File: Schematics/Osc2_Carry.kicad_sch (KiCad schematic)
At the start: 43 parts, among them J16 Conn_01x10h, J17 Screw_Terminal_01x03, J54 Screw_Terminal_01x03, J55 Conn_01x10h, J56 Conn_01x04, J59 Conn_01x04, J60 Conn_01x04, U101 LME49720N, U105 LM358, U12 LM358, U13 TL072, U14 LM358, U15 TL072

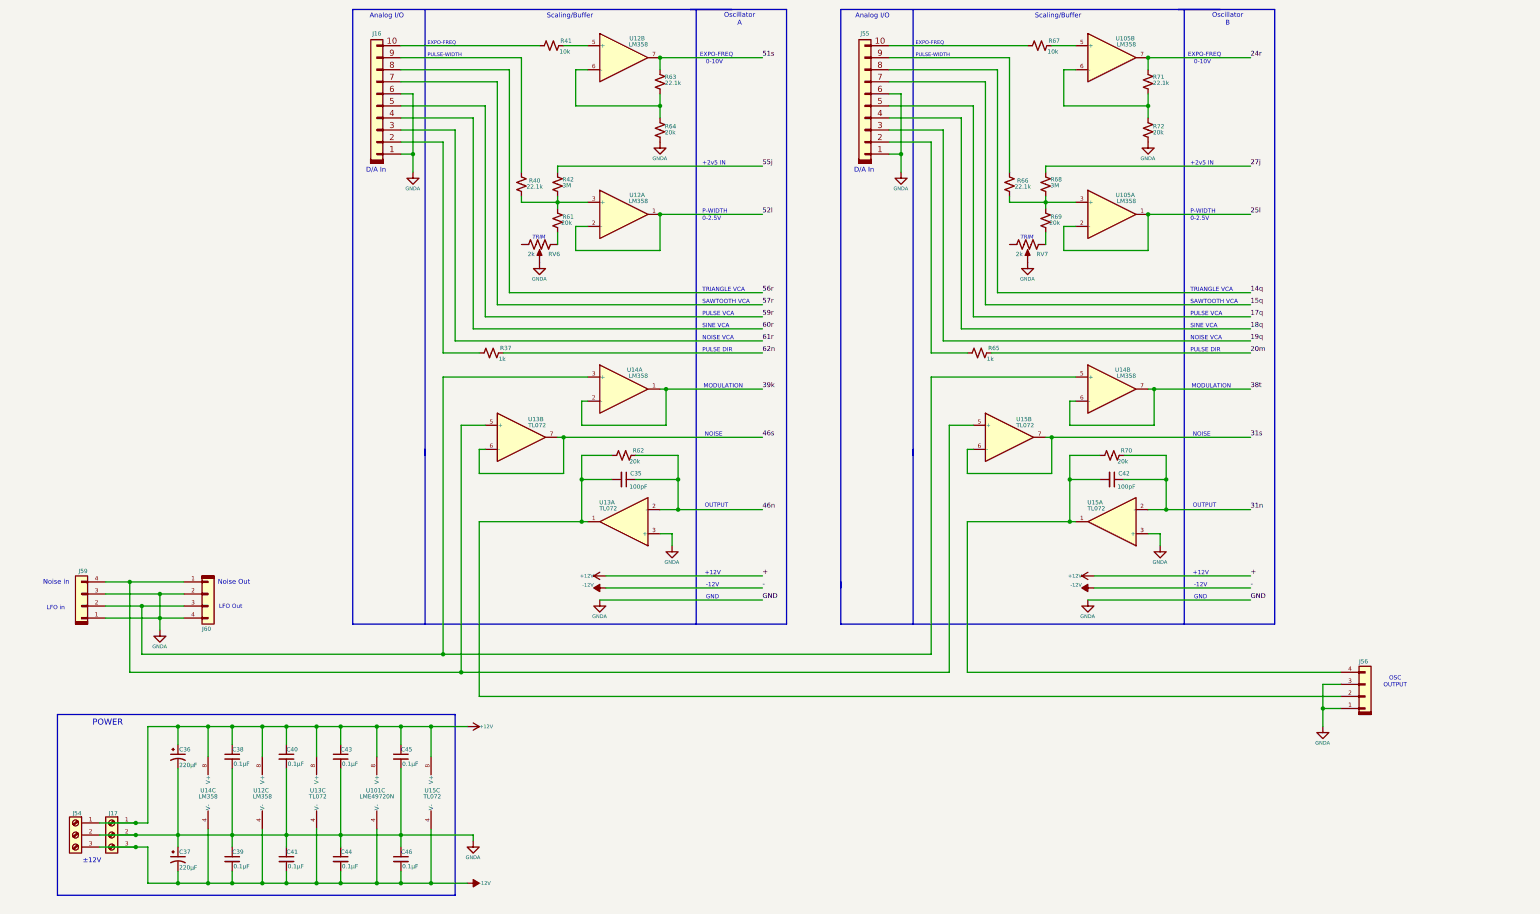
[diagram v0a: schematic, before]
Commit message: Upgreade byte value interface to short.  First stage of refactoring midi input for rotory encoders.  Still needs scaling.
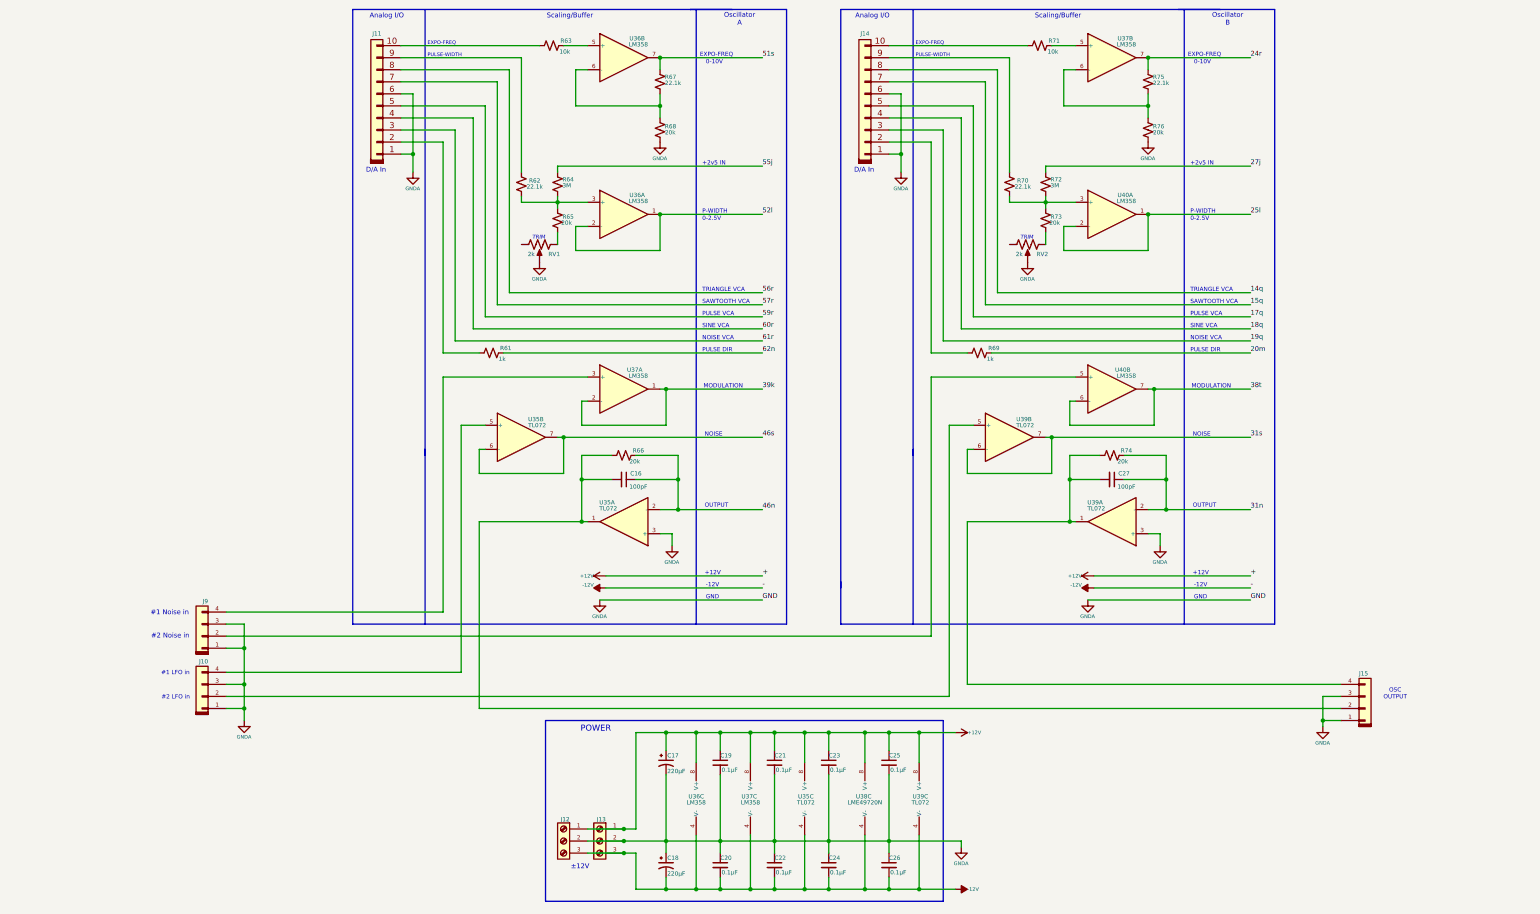
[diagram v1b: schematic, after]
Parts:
- renumbered C35 to C16, C36 to C17, C37 to C18, C38 to C19, C39 to C20, C40 to C21, C41 to C22, C43 to C23, C44 to C24, C45 to C25, C46 to C26, C42 to C27, J59 to J10, J16 to J11, J54 to J12, J17 to J13, J55 to J14, J56 to J15, J60 to J9, R37 to R61, R40 to R62, R41 to R63, R42 to R64, R61 to R65, R62 to R66, R63 to R67, R64 to R68, R65 to R69, R66 to R70, R67 to R71, R68 to R72, R69 to R73, R70 to R74, R71 to R75, R72 to R76, RV6 to RV1, RV7 to RV2, U13 to U35, U14 to U36, U12 to U36, U12 to U37, U105 to U37, U14 to U37, U101 to U38, U15 to U39, U14 to U40, U105 to U40
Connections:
- net GNDA: now also J9.1 (Pin_1), J9.3 (Pin_3); no longer J9.2 (Pin_2), J9.4 (Pin_4)
- net at J10.4 (Pin_4), U35.5 (+): no longer J9.1 (Pin_1), U39.5 (+)
- new net: J9.2 (Pin_2), U40.5 (+)
- new net: J10.2 (Pin_2), U39.5 (+)
- new net: J9.4 (Pin_4), U37.3 (+)
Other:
- note added: "#1 LFO in"
- note added: "#1 Noise in"
- note added: "#2 LFO in"
- note added: "#2 Noise in"
- note removed: "LFO Out"
- note removed: "LFO in"
- note removed: "Noise Out"
- note removed: "Noise in"
- moved on the sheet: C17, C18, C19, C20, C21, C22, C23, C24, C25, C26, J10, J12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

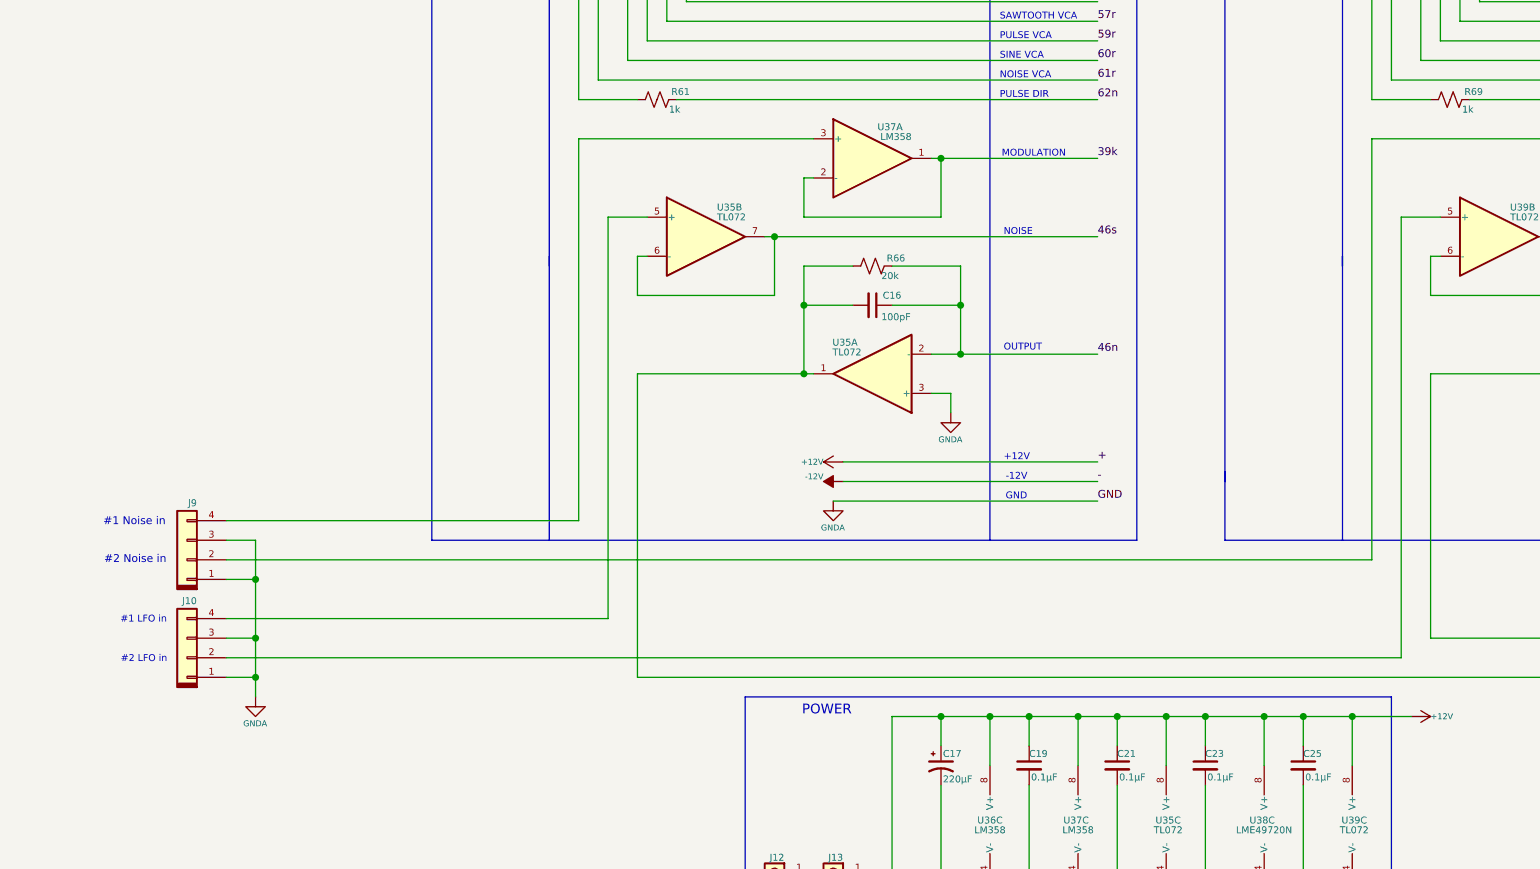
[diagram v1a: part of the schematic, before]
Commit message: Adding in partion LFO-2.  Changed keboard buttons to momentary and encoders to just direction.
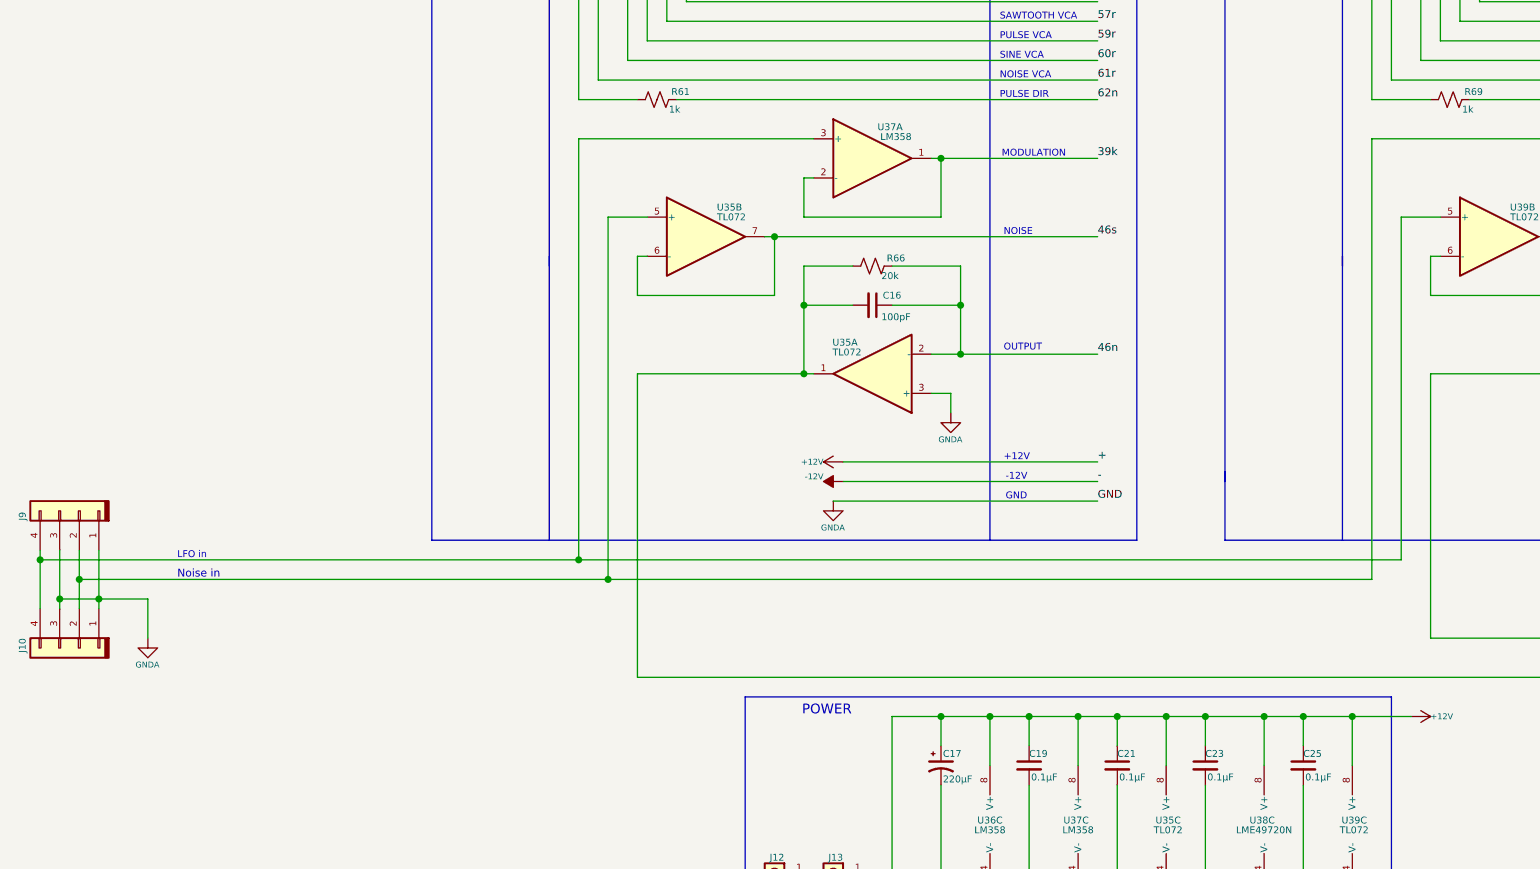
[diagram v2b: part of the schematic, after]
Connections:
- net at U35.5 (+): now also J10.2 (Pin_2), J9.2 (Pin_2), U40.5 (+); no longer J10.4 (Pin_4)
- net at U39.5 (+): now also J10.4 (Pin_4), J9.4 (Pin_4), U37.3 (+); no longer J10.2 (Pin_2)
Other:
- note added: "LFO in"
- note added: "Noise in"
- note removed: "#1 LFO in"
- note removed: "#1 Noise in"
- note removed: "#2 LFO in"
- note removed: "#2 Noise in"
- moved on the sheet: J10, J9

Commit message: Updated schematics including VCO and VCF daughter boards
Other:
- title: (none) -> Dual Oscillator Carrier Module
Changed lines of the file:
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@@
 	(generator_version "8.0")
 	(paper "USLegal")
+	(title_block
+		(title "Dual Oscillator Carrier Module")
+		(date "2025-01-16")
+		(rev "4.4")
+		(comment 1 "In Development ")
+	)
 	(junction
 		(at 133.35 121.92)

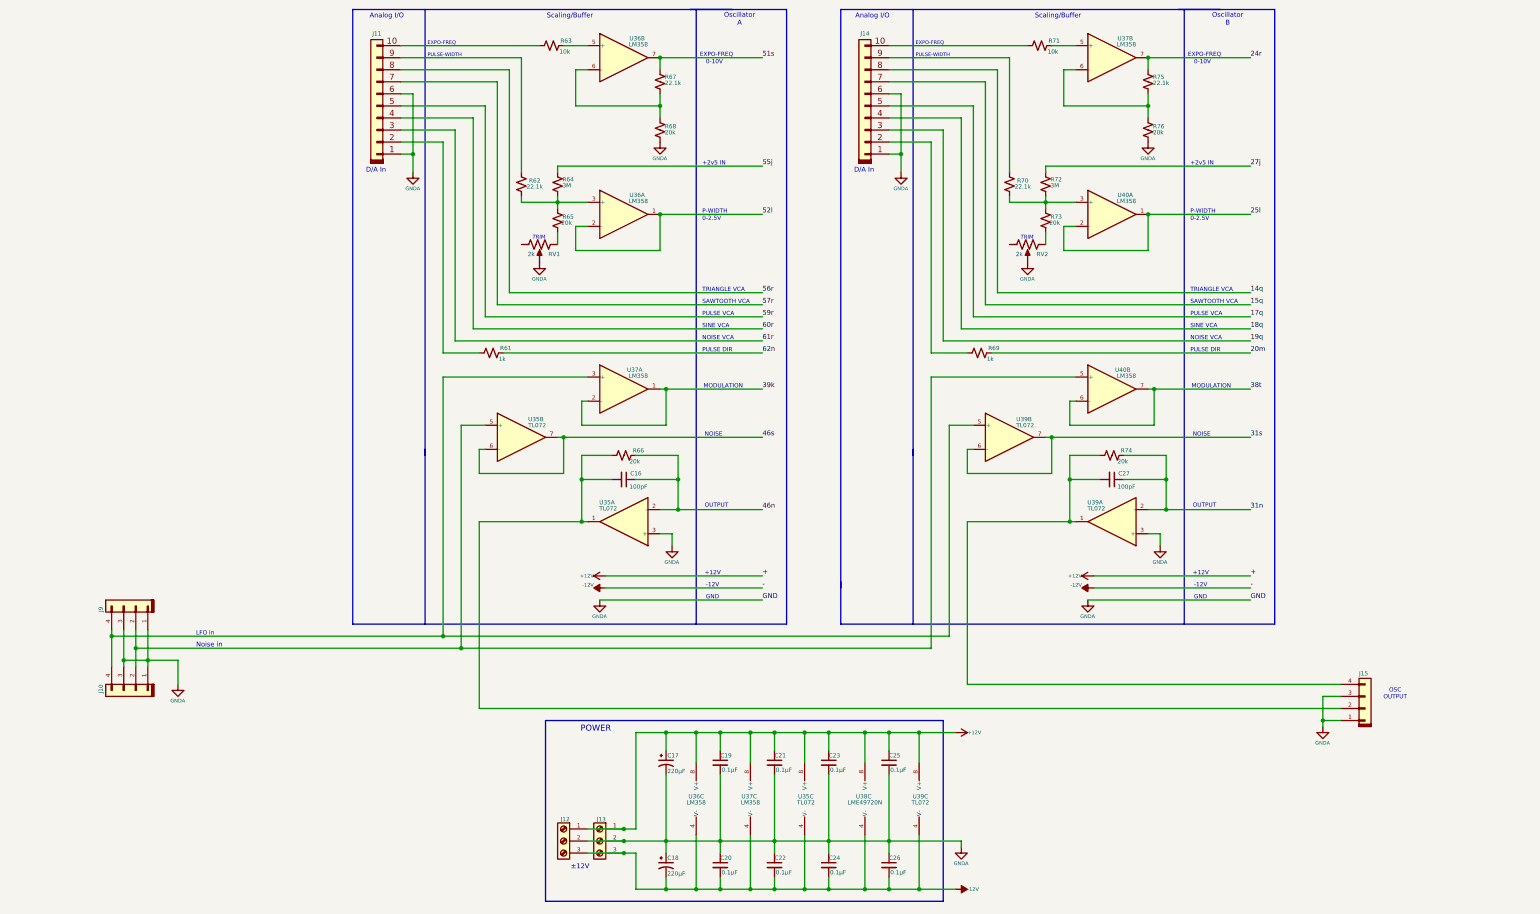
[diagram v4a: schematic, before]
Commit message: All Oscillators have thier own D/A converters and both LFOs are working.  Callibration functions.
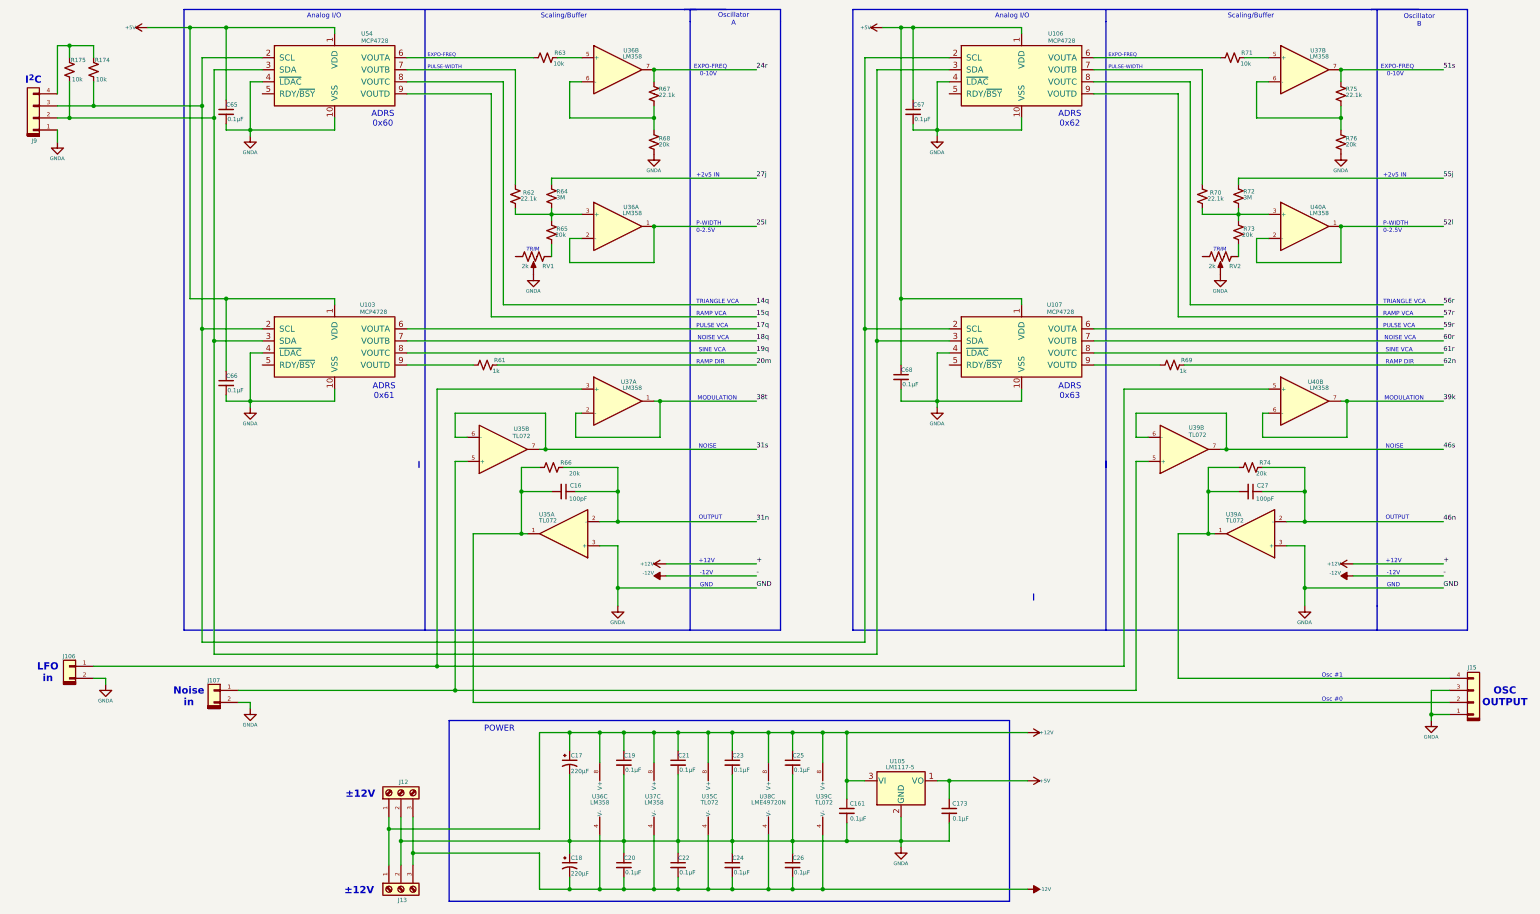
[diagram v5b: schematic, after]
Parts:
- removed J10, J9: Conn_01x04, symbol My Connectors:Conn_01x04
- removed J11, J14: Conn_01x10h, symbol Connector_keyed_kicad_sym:Conn_01x10h
- added C161, C173, C65, C66, C67, C68: 0.1µF, symbol Device:C_Small
- added J106, J107: Conn_01x02, symbol My Connectors:Conn_01x02
- added J9: Conn_01x04, symbol Connector_keyed_kicad_sym:Conn_01x04
- added R174, R175: 10k, symbol Device:R_Small_US
- added U103, U106, U107, U54: MCP4728, Package_SO:MSOP-10_3x3mm_P0.5mm, symbol MyDac:MCP4728
- added U105: LM1117-5, Package_TO_SOT_THT:TO-92_Inline, symbol Regulator_Linear:LM78L05_TO92
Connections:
- net +12V: now also C161.1, U105.3 (VI)
- net 14q: now also U54.8 (VOUTC)
- net 15q: now also U54.9 (VOUTD)
- net 17q: now also U103.6 (VOUTA)
- net 18q: now also U103.7 (VOUTB)
- net 19q: now also U103.8 (VOUTC)
- net 20m: now also R61.2; no longer R69.2
- net 24r: now also R67.1, U36.7; no longer R75.1, U37.7
- net 25l: now also U36.1, U36.2 (-); no longer U40.1, U40.2 (-)
- net 27j: now also R64.1; no longer R72.1
- net 31n: now also C16.1, R66.2, U35.2 (-); no longer C27.1, R74.2, U39.2 (-)
- net 31s: now also U35.6 (-), U35.7; no longer U39.6 (-), U39.7
- net 38t: now also U37.1, U37.2 (-); no longer U40.6 (-), U40.7
- net 39k: now also U40.6 (-), U40.7; no longer U37.1, U37.2 (-)
- net 46n: now also C27.1, R74.2, U39.2 (-); no longer C16.1, R66.2, U35.2 (-)
- net 46s: now also U39.6 (-), U39.7; no longer U35.6 (-), U35.7
- net 51s: now also R75.1, U37.7; no longer R67.1, U36.7
- net 52l: now also U40.1, U40.2 (-); no longer U36.1, U36.2 (-)
- net 55j: now also R72.1; no longer R64.1
- net 56r: now also U106.8 (VOUTC)
- net 57r: now also U106.9 (VOUTD)
- net 59r: now also U107.6 (VOUTA)
- net 60r: now also U107.7 (VOUTB)
- net 61r: now also U107.8 (VOUTC)
- net 62n: now also R69.2; no longer R61.2
- net GNDA: now also C161.2, C173.2, C65.2, C66.2, C67.2, C68.2, J106.2 (Pin_2), J107.2 (Pin_2), J9.1 (Pin_1), U103.10 (VSS), U103.4 (~{LDAC}), U105.2 (GND), U106.10 (VSS), U106.4 (~{LDAC}), U107.10 (VSS), U107.4 (~{LDAC}), U54.10 (VSS), U54.4 (~{LDAC})
- net at U35.5 (+): now also U39.5 (+), J107.1 (Pin_1); no longer U40.5 (+)
- net at R63.1: now also U54.6 (VOUTA)
- net at R71.1: now also U106.6 (VOUTA)
- net at U37.3 (+): now also U40.5 (+), J106.1 (Pin_1); no longer U39.5 (+)
- net at R62.1: now also U54.7 (VOUTB)
- net at R61.1: now also U103.9 (VOUTD)
- net at R70.1: now also U106.7 (VOUTB)
- net at R69.1: now also U107.9 (VOUTD)
- new net: J9.4 (Pin_4), R174.1, R175.1
- new net: J9.3 (Pin_3), R174.2, U103.2 (SCL), U106.2 (SCL), U107.2 (SCL), U54.2 (SCL)
- new net: J9.2 (Pin_2), R175.2, U103.3 (SDA), U106.3 (SDA), U107.3 (SDA), U54.3 (SDA)
- new net +5V: C173.1, C65.1, C66.1, C67.1, C68.1, U103.1 (VDD), U105.1 (VO), U106.1 (VDD), U107.1 (VDD), U54.1 (VDD)
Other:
- note added: "ADRS 0x60"
- note added: "ADRS 0x61"
- note added: "ADRS 0x62"
- note added: "ADRS 0x63"
- note added: "I^{2}C"
- note added: "Osc #0"
- note added: "Osc #1"
- note added: "RAMP DIR"
- note added: "RAMP VCA"
- note removed: "D/A In"
- note removed: "PULSE DIR"
- note removed: "SAWTOOTH VCA"
- moved on the sheet: C16, C17, C18, C19, C20, C21, C22, C23, C24, C25, C26, C27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

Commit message: Fixed bugs in voice selection on configuration.  Reorganized schematics to have different master drawings for power and audio paths.  Started work on dual 3-pole state variable filter with resonance.
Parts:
- renumbered C65 to C33, C66 to C34, C16 to C35, C17 to C36, C18 to C37, C19 to C38, C20 to C39, C21 to C40, C22 to C41, C23 to C42, C24 to C43, C25 to C44, C26 to C45, C161 to C46, C68 to C47, C67 to C48, C173 to C49, C27 to C50, J9 to J40, J106 to J41, J107 to J42, J12 to J43, J13 to J44, J15 to J45, R65 to R10, R66 to R11, R67 to R12, R68 to R14, R69 to R19, R70 to R20, R71 to R21, R72 to R22, R73 to R23, R74 to R24, R75 to R25, R76 to R26, R175 to R3, R174 to R4, R61 to R5, R62 to R6, R63 to R7, R64 to R9, RV1 to RV4, RV2 to RV5, U54 to U21, U103 to U22, U35 to U23, U36 to U24, U37 to U25, U38 to U26, U39 to U27, U105 to U28, U106 to U29, U107 to U30, U40 to U31
